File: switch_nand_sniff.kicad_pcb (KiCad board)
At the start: 2 copper layers, 20.8 x 28.1 mm, 16 parts, among them P1 CONN_02X15, P2 CONN_02X15, P3 CONN_01X08, P4 CONN_01X08

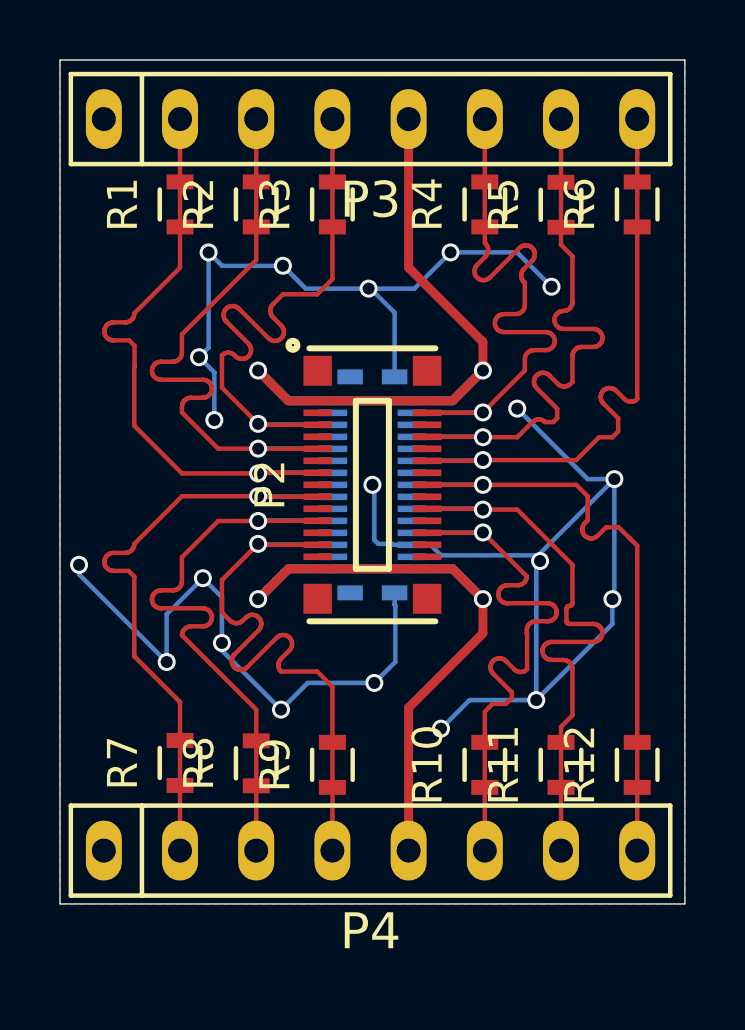
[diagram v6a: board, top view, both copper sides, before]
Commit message: Rev 2 quick cleanup. Added orientation marker, removed unncecessary silkscreen
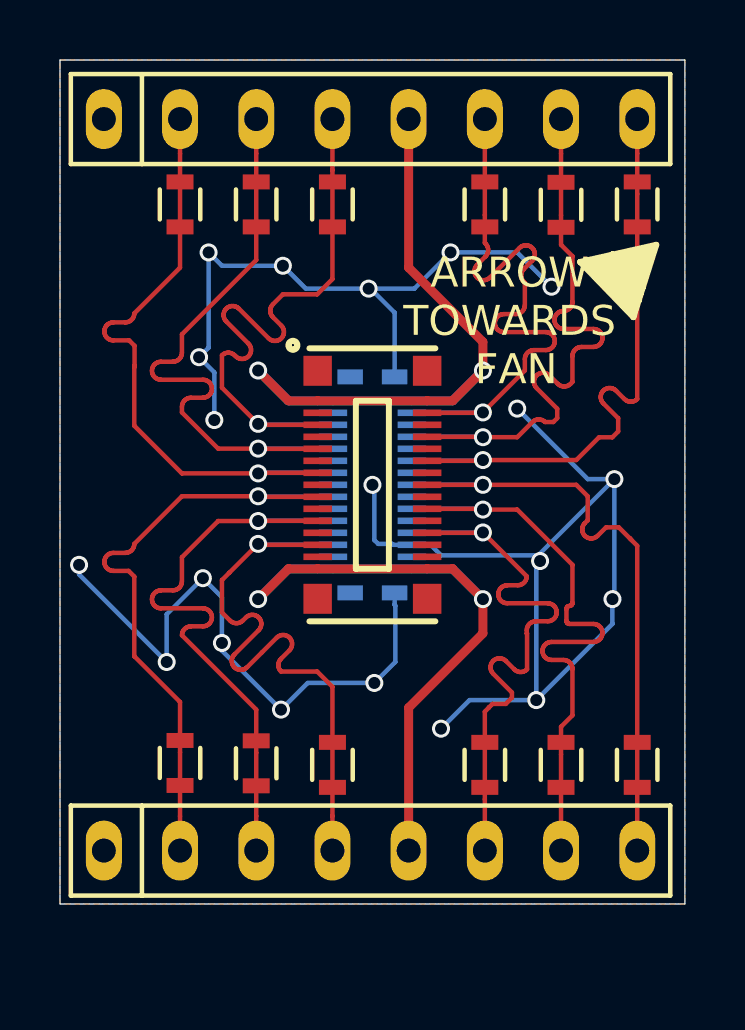
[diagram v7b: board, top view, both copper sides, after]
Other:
- board text added: "ARROW TOWARDS FAN"
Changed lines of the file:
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@@
     (area 125.475499 120.966999 146.304501 149.098501)
     (thickness 1.6)
-    (drawings 4)
+    (drawings 31)
     (tracks 876)
     (zones 0)
@@
     (pad_to_mask_clearance 0)
     (aux_axis_origin 0 0)
-    (visible_elements FFFFFF9F)
+    (visible_elements FFFFFF7F)
     (pcbplotparams
       (layerselection 0x00030_80000001)
@@
     (at 135.889 135.127 270)
     (solder_mask_margin 0.035)
-    (fp_text reference P1 (at 0 -2.75 270) (layer B.SilkS)
+    (fp_text reference P1 (at 0 -2.75 270) (layer B.SilkS) hide
       (effects (font (size 1 1) (thickness 0.15)) (justify mirror))
     )
@@
     (at 135.889 135.127 270)
     (solder_mask_margin 0.035)
-    (fp_text reference P2 (at 0 3.4 270) (layer F.SilkS)
+    (fp_text reference P2 (at 0 3.4 270) (layer F.SilkS) hide
       (effects (font (size 1 1) (thickness 0.15)))
     )
@@
   (module switch:SIP-8 (layer Top)
     (at 135.8265 122.936)
-    (fp_text reference P3 (at 0 2.7) (layer F.SilkS)
+    (fp_text reference P3 (at 0 2.7) (layer F.SilkS) hide
       (effects (font (size 1.2 1.2) (thickness 0.15)))
     )
@@
   (module switch:SIP-8 (layer Top)
     (at 135.8265 147.32)
-    (fp_text reference P4 (at 0 2.7) (layer F.SilkS)
+    (fp_text reference P4 (at 0 2.7) (layer F.SilkS) hide
       (effects (font (size 1.2 1.2) (thickness 0.15)))
     )
@@
     (tags "resistor 0603")
     (attr smd)
-    (fp_text reference R1 (at 0 -1.9 90) (layer F.SilkS)
+    (fp_text reference R1 (at 0 -1.9 90) (layer F.SilkS) hide
       (effects (font (size 1 1) (thickness 0.15)))
     )
@@
     (tags "resistor 0603")
     (attr smd)
-    (fp_text reference R2 (at 0 -1.9 90) (layer F.SilkS)
+    (fp_text reference R2 (at 0 -1.9 90) (layer F.SilkS) hide
       (effects (font (size 1 1) (thickness 0.15)))
     )
@@
     (tags "resistor 0603")
     (attr smd)
-    (fp_text reference R3 (at 0 -1.9 90) (layer F.SilkS)
+    (fp_text reference R3 (at 0 -1.9 90) (layer F.SilkS) hide
       (effects (font (size 1 1) (thickness 0.15)))
     )
@@
     (tags "resistor 0603")
     (attr smd)
-    (fp_text reference R4 (at 0 -1.9 90) (layer F.SilkS)
+    (fp_text reference R4 (at 0 -1.9 90) (layer F.SilkS) hide
       (effects (font (size 1 1) (thickness 0.15)))
     )
@@
     (tags "resistor 0603")
     (attr smd)
-    (fp_text reference R5 (at 0 -1.9 90) (layer F.SilkS)
+    (fp_text reference R5 (at 0 -1.9 90) (layer F.SilkS) hide
       (effects (font (size 1 1) (thickness 0.15)))
     )
@@
     (tags "resistor 0603")
     (attr smd)
-    (fp_text reference R6 (at 0 -1.9 90) (layer F.SilkS)
+    (fp_text reference R6 (at 0 -1.9 90) (layer F.SilkS) hide
       (effects (font (size 1 1) (thickness 0.15)))
     )
@@
     (tags "resistor 0603")
     (attr smd)
-    (fp_text reference R7 (at 0 -1.9 90) (layer F.SilkS)
+    (fp_text reference R7 (at 0 -1.9 90) (layer F.SilkS) hide
       (effects (font (size 1 1) (thickness 0.15)))
     )
@@
     (tags "resistor 0603")
     (attr smd)
-    (fp_text reference R8 (at 0 -1.9 90) (layer F.SilkS)
+    (fp_text reference R8 (at 0 -1.9 90) (layer F.SilkS) hide
       (effects (font (size 1 1) (thickness 0.15)))
     )
@@
     (tags "resistor 0603")
     (attr smd)
-    (fp_text reference R9 (at 0 -1.9 90) (layer F.SilkS)
+    (fp_text reference R9 (at 0 -1.9 90) (layer F.SilkS) hide
       (effects (font (size 1 1) (thickness 0.15)))
     )
@@
     (tags "resistor 0603")
     (attr smd)
-    (fp_text reference R10 (at 0 -1.9 90) (layer F.SilkS)
+    (fp_text reference R10 (at 0 -1.9 90) (layer F.SilkS) hide
       (effects (font (size 1 1) (thickness 0.15)))
     )
@@
     (tags "resistor 0603")
     (attr smd)
-    (fp_text reference R11 (at 0 -1.9 90) (layer F.SilkS)
+    (fp_text reference R11 (at 0 -1.9 90) (layer F.SilkS) hide
       (effects (font (size 1 1) (thickness 0.15)))
     )
@@
     (tags "resistor 0603")
     (attr smd)
-    (fp_text reference R12 (at 0 -1.9 90) (layer F.SilkS)
+    (fp_text reference R12 (at 0 -1.9 90) (layer F.SilkS) hide
       (effects (font (size 1 1) (thickness 0.15)))
     )
@@
     )
   )
+  (gr_text "ARROW \nTOWARDS\n FAN" (at 140.462 129.667) (layer F.SilkS)
+    (effects (font (size 1 1) (thickness 0.1)))
+  )
+  (gr_line (start 144.907 127.254) (end 145.2245 127.3175) (layer F.SilkS) (width 0.2))
+  (gr_line (start 145.161 127.5715) (end 144.907 127.254) (layer F.SilkS) (width 0.2))
+  (gr_line (start 144.653 127.3175) (end 145.161 127.5715) (layer F.SilkS) (width 0.2))
+  (gr_line (start 145.0975 127.8255) (end 144.653 127.3175) (layer F.SilkS) (width 0.2))
+  (gr_line (start 144.526 127.381) (end 145.0975 127.8255) (layer F.SilkS) (width 0.2))
+  (gr_line (start 145.034 128.016) (end 144.526 127.381) (layer F.SilkS) (width 0.2))
+  (gr_line (start 144.3355 127.4445) (end 145.034 128.016) (layer F.SilkS) (width 0.2))
+  (gr_line (start 144.9705 128.2065) (end 144.3355 127.4445) (layer F.SilkS) (width 0.2))
+  (gr_line (start 144.0815 127.4445) (end 144.9705 128.2065) (layer F.SilkS) (width 0.2))
+  (gr_line (start 144.8435 128.27) (end 144.0815 127.4445) (layer F.SilkS) (width 0.2))
+  (gr_line (start 143.891 127.5715) (end 144.8435 128.27) (layer F.SilkS) (width 0.2))
+  (gr_line (start 144.907 128.524) (end 143.891 127.5715) (layer F.SilkS) (width 0.2))
+  (gr_line (start 143.891 127.4445) (end 144.907 128.524) (layer F.SilkS) (width 0.2))
+  (gr_line (start 144.8435 128.7145) (end 143.891 127.4445) (layer F.SilkS) (width 0.2))
+  (gr_line (start 143.7005 127.5715) (end 144.8435 128.7145) (layer F.SilkS) (width 0.2))
+  (gr_line (start 144.78 128.9685) (end 143.7005 127.5715) (layer F.SilkS) (width 0.2))
+  (gr_line (start 143.51 127.635) (end 144.78 128.9685) (layer F.SilkS) (width 0.2))
+  (gr_line (start 144.653 129.032) (end 143.51 127.635) (layer F.SilkS) (width 0.2))
+  (gr_line (start 143.3195 127.6985) (end 144.653 129.032) (layer F.SilkS) (width 0.2))
+  (gr_line (start 144.5895 129.2225) (end 143.3195 127.6985) (layer F.SilkS) (width 0.2))
+  (gr_line (start 143.0655 127.635) (end 144.5895 129.2225) (layer F.SilkS) (width 0.2))
+  (gr_line (start 143.0655 127.762) (end 143.0655 127.635) (layer F.SilkS) (width 0.2))
+  (gr_line (start 144.5895 129.413) (end 143.0655 127.762) (layer F.SilkS) (width 0.2))
+  (gr_line (start 145.3515 127.127) (end 142.8115 127.6985) (layer F.SilkS) (width 0.2))
+  (gr_line (start 144.5895 129.54) (end 145.3515 127.127) (layer F.SilkS) (width 0.2))
+  (gr_line (start 142.8115 127.6985) (end 144.5895 129.54) (layer F.SilkS) (width 0.2))
   (gr_line (start 146.304 149.098) (end 146.304 120.9675) (layer Edge.Cuts) (width 0.001))
   (gr_line (start 146.304 120.9675) (end 125.476 120.9675) (layer Edge.Cuts) (width 0.001))

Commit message: Added some fun silkscreen touches. now rev 2.2
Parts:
- added G***: LOGO, switch:open_hw_logo, F.Cu at (143.9, 141.4)
- added G***: LOGO, switch:rs_logo, F.Cu at (128.1, 129.0)
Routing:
- net GND: track 74.2 -> 75.1 mm
- net (no net): track 0.92 -> 0.00 mm
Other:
- board text added: "HACk-eMMC by hedgeberg"
